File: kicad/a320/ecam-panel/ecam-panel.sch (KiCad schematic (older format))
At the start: 45 parts, among them P1 CONN_02X04, SW1 SW_PUSH_SMALL, SW10 SW_PUSH_SMALL, SW11 SW_PUSH_SMALL, SW12 SW_PUSH_SMALL, SW13 SW_PUSH_SMALL, SW14 SW_PUSH_SMALL, SW15 SW_PUSH_SMALL, SW16 SW_PUSH_SMALL, SW17 SW_PUSH_SMALL_H, SW18 SW_PUSH_SMALL_H, SW2 SW_PUSH_SMALL, SW3 SW_PUSH_SMALL, SW4 SW_PUSH_SMALL, SW5 SW_PUSH_SMALL, SW6 SW_PUSH_SMALL, SW7 SW_PUSH_SMALL, SW8 SW_PUSH_SMALL, SW9 SW_PUSH_SMALL, U1 CD4021, U2 74922, U3 MAX7219

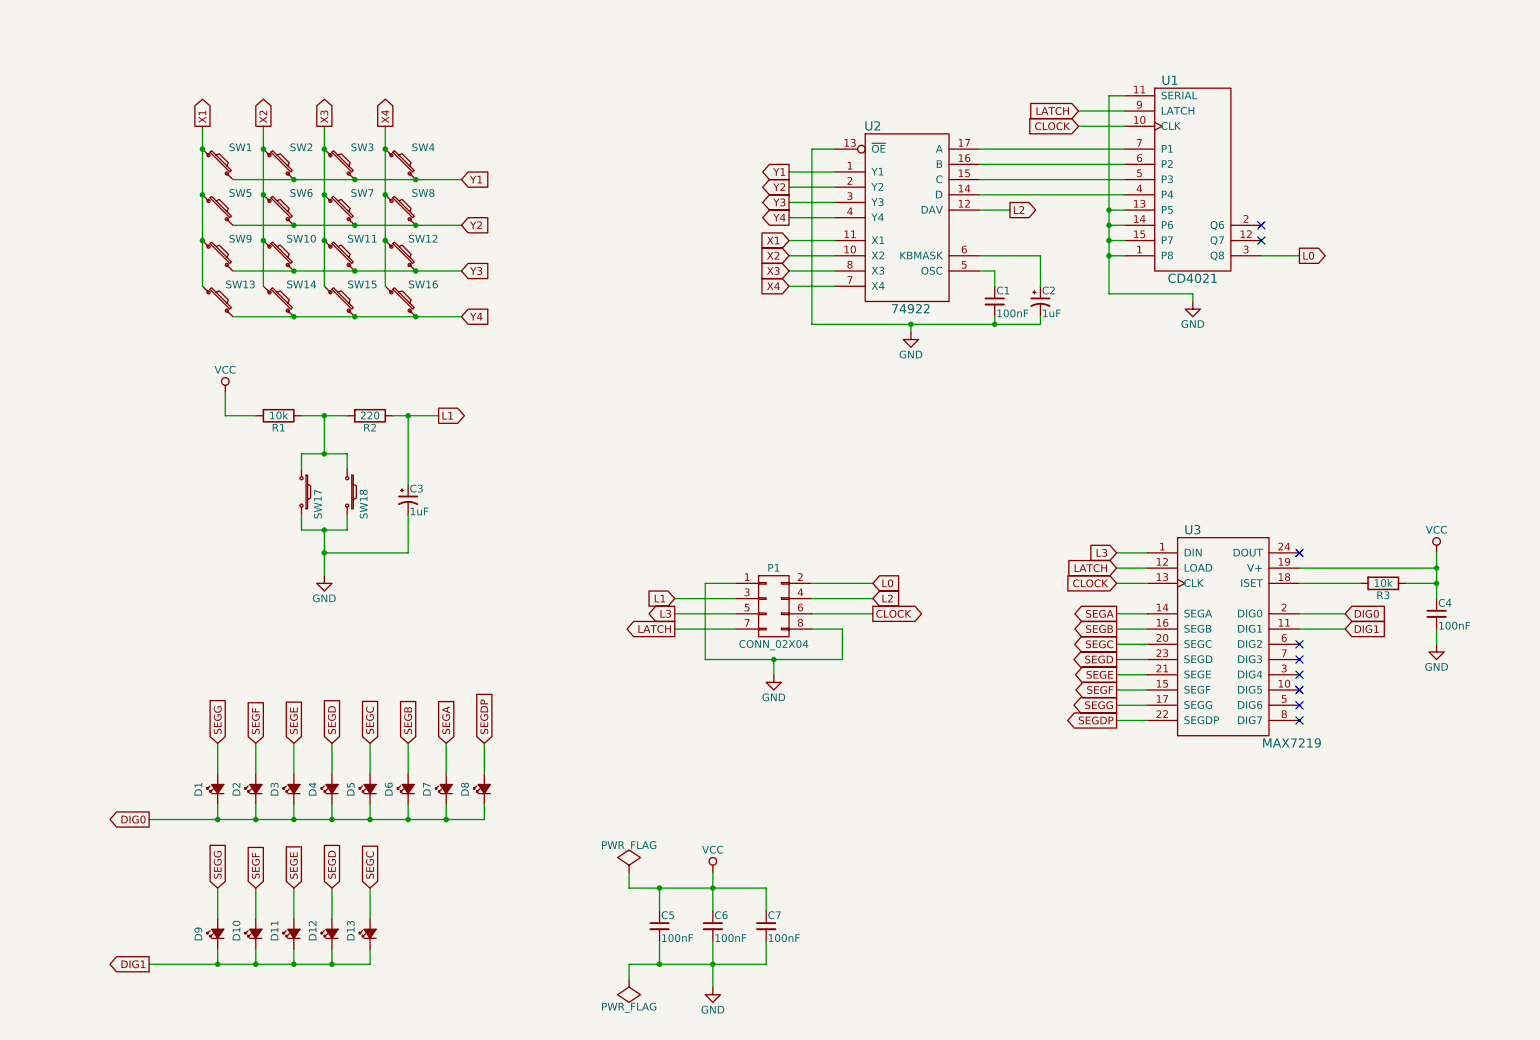
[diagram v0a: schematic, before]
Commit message: Add potentiometers to control ECAM display bright
And also, reorganize the schematic to separate the different subsets of components.
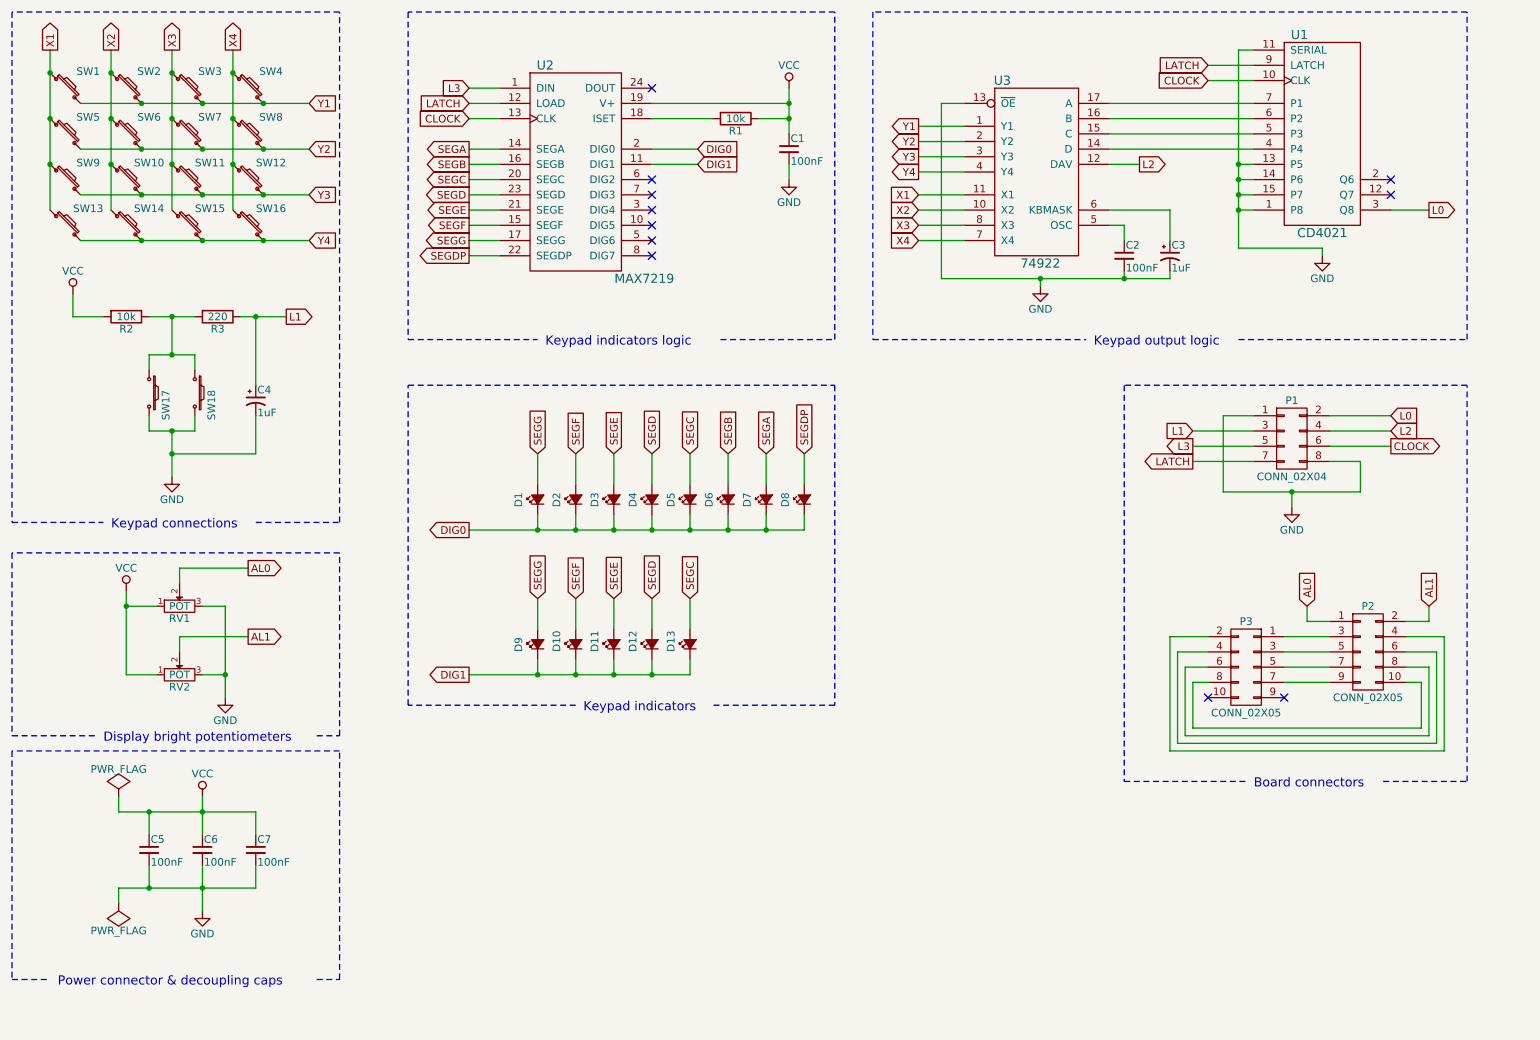
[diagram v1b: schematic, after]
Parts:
- added P2, P3: CONN_02X05, symbol CONN_02X05
- added RV1, RV2: POT, symbol POT
- renumbered C4 to C1, C1 to C2, C2 to C3, C3 to C4, R3 to R1, R1 to R2, R2 to R3, U3 to U2, U2 to U3
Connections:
- net GND: now also RV1.3, RV2.3
- net VCC: now also RV1.1, RV2.1
- new net: P2.10 (P10), P3.8 (P8)
- new net: P2.3 (P3), P3.1 (P1)
- new net: P2.4 (P4), P3.2 (P2)
- new net: P2.5 (P5), P3.3 (P3)
- new net: P2.6 (P6), P3.4 (P4)
- new net: P2.7 (P7), P3.5 (P5)
- new net: P2.8 (P8), P3.6 (P6)
- new net: P2.9 (P9), P3.7 (P7)
- new net AL0: P2.1 (P1), RV1.2
- new net AL1: P2.2 (P2), RV2.2
- no-connect marks 9 -> 11
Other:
- note added: "Board connectors"
- note added: "Display bright potentiometers"
- note added: "Keypad connections"
- note added: "Keypad indicators"
- note added: "Keypad indicators logic"
- note added: "Keypad output logic"
- note added: "Power connector & decoupling caps"
- moved on the sheet: C1, C2, C3, C4, C5, C6, C7, D1, D10, D11, D12, D13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

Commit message: Add backlighting LEDs and power connectors to ECAM panel
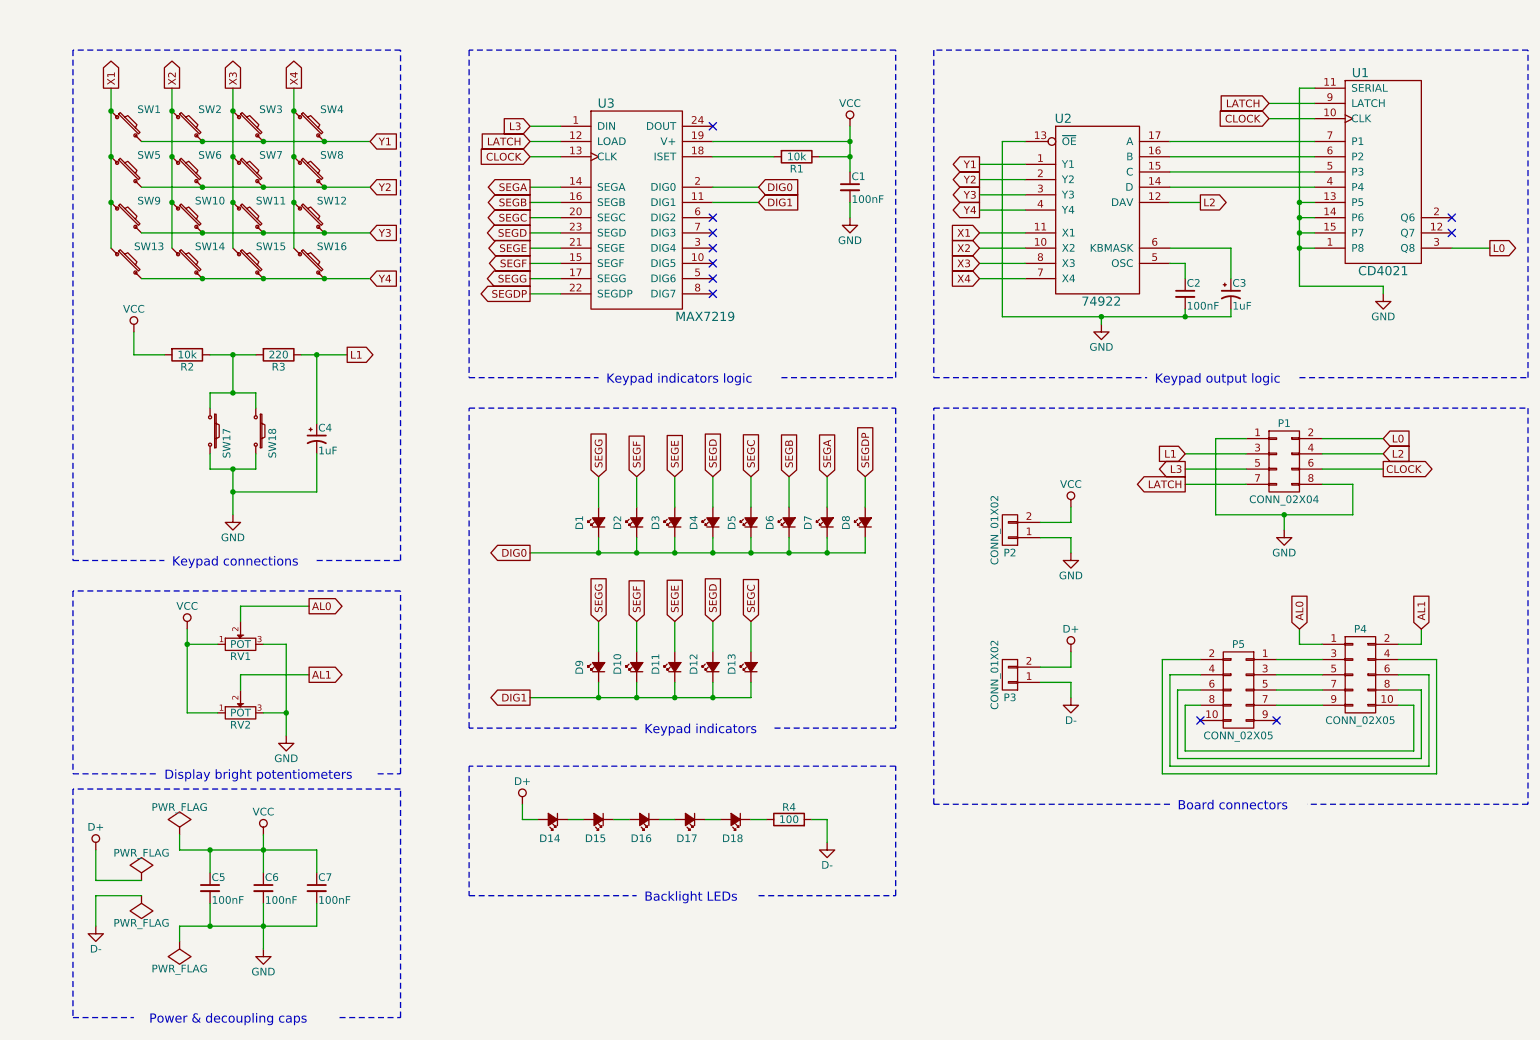
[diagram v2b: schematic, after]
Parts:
- added D14, D15, D16, D17, D18: Led_Small, symbol Led_Small
- added P2, P3: CONN_01X02, symbol CONN_01X02
- added R4: 100, symbol R
- renumbered P2 to P4, P3 to P5, U3 to U2, U2 to U3
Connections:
- net GND: now also P2.1 (P1)
- net VCC: now also P2.2 (P2)
- new net: D14.1 (K), D15.2 (A)
- new net: D15.1 (K), D16.2 (A)
- new net: D16.1 (K), D17.2 (A)
- new net: D18.1 (K), R4.1
- new net: D17.1 (K), D18.2 (A)
- new net D+: D14.2 (A), P3.2 (P2)
- new net D-: P3.1 (P1), R4.2
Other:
- note added: "Backlight LEDs"
- note added: "Power & decoupling caps"
- note removed: "Power connector & decoupling caps"
- moved on the sheet: C1, C2, C3, C4, C5, C6, C7, D1, D10, D11, D12, D13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

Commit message: Add some associations to footprints in A320 ECAM panel
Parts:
- C1, C2, C5, C6, C7: footprint (none) -> avionica:Disc_capacitor
- C3, C4: footprint (none) -> avionica:Radial_capacitor
- D1, D10, D11, D12, D13, D2, D3, D4, D5, D6, D7, D8, D9: footprint (none) -> avionica:Pin_Header_1x02
- D14, D15, D16, D17, D18: footprint (none) -> avionica:LED-1210
- P1: footprint (none) -> avionica:idc-8p
- P4, P5: footprint (none) -> avionica:idc-10p
- R1, R2, R3, R4: footprint (none) -> avionica:Axial_resistor
- RV1, RV2: footprint (none) -> avionica:Pin_Header_1x03
- SW1, SW10, SW11, SW12, SW13, SW14, SW15, SW16, SW17, SW18, SW2, SW3, SW4, SW5, SW6, SW7, SW8, SW9: footprint (none) -> avionica:Omron-B3F-12mm

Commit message: Replace power connectors by 3-line ones
One for anode, two for cathode.
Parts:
- removed P2, P3: CONN_01X02, symbol CONN_01X02
- added P2, P3: CONN_01X03, symbol CONN_01X03
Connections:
- net D+: now also P3.1 (P1)
- net D-: now also P3.2 (P2), P3.3 (P3)
- net GND: now also P2.2 (P2), P2.3 (P3)
- net VCC: now also P2.1 (P1)
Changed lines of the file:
@@
 	3800 6500 4900 6500
-$Comp
-L CONN_01X02 P2
-U 1 1 596968F2
-P 7350 4100
-F 0 "P2" H 7350 4250 50  0000 C CNN
-F 1 "CONN_01X02" V 7450 4100 50  0000 C CNN
-F 2 "" H 7350 4100 50  0001 C CNN
-F 3 "" H 7350 4100 50  0000 C CNN
-	1    7350 4100
-	-1   0    0    1
-$EndComp
-$Comp
-L CONN_01X02 P3
-U 1 1 596969E3
-P 7350 5050
-F 0 "P3" H 7350 5200 50  0000 C CNN
-F 1 "CONN_01X02" V 7450 5050 50  0000 C CNN
-F 2 "" H 7350 5050 50  0001 C CNN
-F 3 "" H 7350 5050 50  0000 C CNN
-	1    7350 5050
-	-1   0    0    1
-$EndComp
 $Comp
 L VCC #PWR020
@@
 L GND #PWR021
 U 1 1 59696FAF
-P 7750 4250
-F 0 "#PWR021" H 7750 4000 50  0001 C CNN
-F 1 "GND" H 7750 4100 50  0000 C CNN
-F 2 "" H 7750 4250 50  0000 C CNN
-F 3 "" H 7750 4250 50  0000 C CNN
-	1    7750 4250
+P 7750 4400
+F 0 "#PWR021" H 7750 4150 50  0001 C CNN
+F 1 "GND" H 7750 4250 50  0000 C CNN
+F 2 "" H 7750 4400 50  0000 C CNN
+F 3 "" H 7750 4400 50  0000 C CNN
+	1    7750 4400
 	1    0    0    -1
 $EndComp
@@
 L D- #PWR023
 U 1 1 5969711B
-P 7750 5200
-F 0 "#PWR023" H 7750 4950 50  0001 C CNN
-F 1 "D-" H 7750 5050 50  0000 C CNN
-F 2 "" H 7750 5200 50  0000 C CNN
-F 3 "" H 7750 5200 50  0000 C CNN
-	1    7750 5200
+P 7750 5350
+F 0 "#PWR023" H 7750 5100 50  0001 C CNN
+F 1 "D-" H 7750 5200 50  0000 C CNN
+F 2 "" H 7750 5350 50  0000 C CNN
+F 3 "" H 7750 5350 50  0000 C CNN
+	1    7750 5350
 	1    0    0    -1
 $EndComp
@@
 	7550 4150 7750 4150
 Wire Wire Line
-	7750 4150 7750 4250
+	7750 4150 7750 4400
 Wire Wire Line
 	7750 3950 7750 4050
@@
 	7550 5100 7750 5100
 Wire Wire Line
-	7750 5100 7750 5200
+	7750 5100 7750 5350
 Wire Notes Line
 	6850 5900 6850 3300
@@
 Wire Notes Line
 	8400 5900 6850 5900
+$Comp
+L CONN_01X03 P2
+U 1 1 5968BBC7
+P 7350 4150
+F 0 "P2" H 7350 4350 50  0000 C CNN
+F 1 "CONN_01X03" V 7450 4150 50  0000 C CNN
+F 2 "" H 7350 4150 50  0000 C CNN
+F 3 "" H 7350 4150 50  0000 C CNN
+	1    7350 4150
+	-1   0    0    -1
+$EndComp
+$Comp
+L CONN_01X03 P3
+U 1 1 5968BDE2
+P 7350 5100
+F 0 "P3" H 7350 5300 50  0000 C CNN
+F 1 "CONN_01X03" V 7450 5100 50  0000 C CNN
+F 2 "" H 7350 5100 50  0000 C CNN
+F 3 "" H 7350 5100 50  0000 C CNN
+	1    7350 5100
+	-1   0    0    -1
+$EndComp
+Wire Wire Line
+	7750 4250 7550 4250
+Connection ~ 7750 4250
+Wire Wire Line
+	7550 5200 7750 5200
+Connection ~ 7750 5200
 $EndSCHEMATC

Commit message: Add the remaining footprint associations in A320 ECAM panel
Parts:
- P2, P3: footprint (none) -> avionica:Jack_55_21
- U1: footprint (none) -> avionica:DIP-16
- U2: footprint (none) -> avionica:DIP-18
- U3: footprint (none) -> avionica:DIP-24
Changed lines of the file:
@@
 F 0 "U3" H 4700 3100 60  0000 C CNN
 F 1 "MAX7219" H 5350 1700 60  0000 C CNN
-F 2 "" H 5050 1400 60  0001 C CNN
+F 2 "avionica:DIP-24" H 5050 1400 60  0001 C CNN
 F 3 "" H 5050 1400 60  0001 C CNN
 	1    4900 2200
@@
 F 0 "U2" H 7700 2800 60  0000 C CNN
 F 1 "74922" H 7950 1600 60  0000 C CNN
-F 2 "" H 7950 2100 60  0001 C CNN
+F 2 "avionica:DIP-18" H 7950 2100 60  0001 C CNN
 F 3 "" H 7950 2100 60  0001 C CNN
 	1    7950 2100
@@
 F 0 "U1" H 9650 2400 60  0000 C CNN
 F 1 "CD4021" H 9800 1100 60  0000 C CNN
-F 2 "" H 9750 1550 60  0001 C CNN
+F 2 "avionica:DIP-16" H 9750 1550 60  0001 C CNN
 F 3 "" H 9750 1550 60  0001 C CNN
 	1    9800 1750
@@
 F 0 "P2" H 7350 4350 50  0000 C CNN
 F 1 "CONN_01X03" V 7450 4150 50  0000 C CNN
-F 2 "" H 7350 4150 50  0000 C CNN
+F 2 "avionica:Jack_55_21" H 7350 4150 50  0001 C CNN
 F 3 "" H 7350 4150 50  0000 C CNN
 	1    7350 4150
@@
 F 0 "P3" H 7350 5300 50  0000 C CNN
 F 1 "CONN_01X03" V 7450 5100 50  0000 C CNN
-F 2 "" H 7350 5100 50  0000 C CNN
+F 2 "avionica:Jack_55_21" H 7350 5100 50  0001 C CNN
 F 3 "" H 7350 5100 50  0000 C CNN
 	1    7350 5100

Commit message: Make the VCC pin non-visible in MAX7219
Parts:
- removed C1: 100nF, avionica:Disc_capacitor, symbol C_Small
- renumbered C2 to C1, C3 to C2, C4 to C3, C5 to C4, C6 to C5, C7 to C6
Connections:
- net VCC: no longer U3.19 (V+)
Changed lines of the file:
@@
 Y4
 $Comp
-L C_Small C2
+L C_Small C1
 U 1 1 5951E730
 P 8500 2550
-F 0 "C2" H 8510 2620 50  0000 L CNN
+F 0 "C1" H 8510 2620 50  0000 L CNN
 F 1 "100nF" H 8510 2470 50  0000 L CNN
 F 2 "avionica:Disc_capacitor" H 8500 2550 50  0001 C CNN
@@
 	0    1    1    0
 $EndComp
-$Comp
-L C_Small C1
-U 1 1 5952D81F
-P 6300 1850
-F 0 "C1" H 6310 1920 50  0000 L CNN
-F 1 "100nF" H 6310 1770 50  0000 L CNN
-F 2 "avionica:Disc_capacitor" H 6300 1850 50  0001 C CNN
-F 3 "" H 6300 1850 50  0000 C CNN
-	1    6300 1850
-	1    0    0    -1
-$EndComp
-Wire Wire Line
-	6300 2050 6300 1950
-Wire Wire Line
-	6300 1450 6300 1750
 Wire Wire Line
 	6300 1650 6100 1650
 Wire Wire Line
 	5800 1650 5400 1650
-Wire Wire Line
-	5400 1550 6300 1550
-Connection ~ 6300 1650
-Connection ~ 6300 1550
 $Comp
 L SW_PUSH_SMALL_H SW18
@@
 Connection ~ 9250 1950
 $Comp
-L C_Small C6
+L C_Small C5
 U 1 1 5953F9B6
 P 2450 6450
-F 0 "C6" H 2460 6520 50  0000 L CNN
+F 0 "C5" H 2460 6520 50  0000 L CNN
 F 1 "100nF" H 2460 6370 50  0000 L CNN
 F 2 "avionica:Disc_capacitor" H 2450 6450 50  0001 C CNN
@@
 $EndComp
 $Comp
-L C_Small C5
+L C_Small C4
 U 1 1 5953FC97
 P 2100 6450
-F 0 "C5" H 2110 6520 50  0000 L CNN
+F 0 "C4" H 2110 6520 50  0000 L CNN
 F 1 "100nF" H 2110 6370 50  0000 L CNN
 F 2 "avionica:Disc_capacitor" H 2100 6450 50  0001 C CNN
@@
 $EndComp
 $Comp
-L C_Small C7
+L C_Small C6
 U 1 1 5953FD35
 P 2800 6450
-F 0 "C7" H 2810 6520 50  0000 L CNN
+F 0 "C6" H 2810 6520 50  0000 L CNN
 F 1 "100nF" H 2810 6370 50  0000 L CNN
 F 2 "avionica:Disc_capacitor" H 2800 6450 50  0001 C CNN
@@
 $EndComp
 $Comp
-L GND #PWR010
-U 1 1 59543FF4
-P 6300 2050
-F 0 "#PWR010" H 6300 1800 50  0001 C CNN
-F 1 "GND" H 6300 1900 50  0000 C CNN
-F 2 "" H 6300 2050 50  0000 C CNN
-F 3 "" H 6300 2050 50  0000 C CNN
-	1    6300 2050
-	1    0    0    -1
-$EndComp
-$Comp
 L VCC #PWR011
 U 1 1 595440B4
@@
 $EndComp
 $Comp
-L CP1_Small C4
+L CP1_Small C3
 U 1 1 595770B6
 P 2800 3500
-F 0 "C4" H 2810 3570 50  0000 L CNN
+F 0 "C3" H 2810 3570 50  0000 L CNN
 F 1 "1uF" H 2810 3420 50  0000 L CNN
 F 2 "avionica:Radial_capacitor" H 2800 3500 50  0001 C CNN
@@
 $EndComp
 $Comp
-L CP1_Small C3
+L CP1_Small C2
 U 1 1 5958C1F6
 P 8800 2550
-F 0 "C3" H 8810 2620 50  0000 L CNN
+F 0 "C2" H 8810 2620 50  0000 L CNN
 F 1 "1uF" H 8810 2470 50  0000 L CNN
 F 2 "avionica:Radial_capacitor" H 8800 2550 50  0001 C CNN
@@
 	1    0    0    -1
 $EndComp
+Wire Wire Line
+	6300 1650 6300 1450
 $EndSCHEMATC

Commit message: Adjust footprints layout in A320 ECAM panel
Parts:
- added D14: Led_Small, avionica:Pin_Header_1x02, symbol Led_Small
- renumbered D14 to D15, D15 to D16, D16 to D17, D17 to D18, D18 to D19
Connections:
- net DIG1: now also D14.1 (K)
- net SEGB: now also D14.2 (A)
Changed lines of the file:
@@
 LIBS:contrib
 LIBS:valves
-LIBS:ecam-panel-cache
 EELAYER 25 0
 EELAYER END
@@
 	5650 5200 5650 5100
 Wire Wire Line
-	4200 5200 5650 5200
+	4200 5200 5900 5200
 Wire Wire Line
 	5400 5100 5400 5200
@@
 	9250 3100 10750 3100
 $Comp
-L Led_Small D14
+L Led_Small D15
 U 1 1 59682439
 P 4350 6000
-F 0 "D14" H 4300 6125 50  0000 L CNN
+F 0 "D15" H 4300 6125 50  0000 L CNN
 F 1 "Led_Small" H 4175 5900 50  0001 L CNN
 F 2 "avionica:LED-1210" V 4350 6000 50  0001 C CNN
@@
 $EndComp
 $Comp
-L Led_Small D15
+L Led_Small D16
 U 1 1 59687653
 P 4650 6000
-F 0 "D15" H 4600 6125 50  0000 L CNN
+F 0 "D16" H 4600 6125 50  0000 L CNN
 F 1 "Led_Small" H 4475 5900 50  0001 L CNN
 F 2 "avionica:LED-1210" V 4650 6000 50  0001 C CNN
@@
 $EndComp
 $Comp
-L Led_Small D16
+L Led_Small D17
 U 1 1 5968770B
 P 4950 6000
-F 0 "D16" H 4900 6125 50  0000 L CNN
+F 0 "D17" H 4900 6125 50  0000 L CNN
 F 1 "Led_Small" H 4775 5900 50  0001 L CNN
 F 2 "avionica:LED-1210" V 4950 6000 50  0001 C CNN
@@
 	6150 6000 6050 6000
 $Comp
-L Led_Small D17
+L Led_Small D18
 U 1 1 59689C60
 P 5250 6000
-F 0 "D17" H 5200 6125 50  0000 L CNN
+F 0 "D18" H 5200 6125 50  0000 L CNN
 F 1 "Led_Small" H 5075 5900 50  0001 L CNN
 F 2 "avionica:LED-1210" V 5250 6000 50  0001 C CNN
@@
 $EndComp
 $Comp
-L Led_Small D18
+L Led_Small D19
 U 1 1 59689D1E
 P 5550 6000
-F 0 "D18" H 5500 6125 50  0000 L CNN
+F 0 "D19" H 5500 6125 50  0000 L CNN
 F 1 "Led_Small" H 5375 5900 50  0001 L CNN
 F 2 "avionica:LED-1210" V 5550 6000 50  0001 C CNN
@@
 Wire Wire Line
 	6300 1650 6300 1450
+Text GLabel 5900 4700 1    50   Input ~ 0
+SEGB
+$Comp
+L Led_Small D14
+U 1 1 597B8575
+P 5900 5000
+F 0 "D14" H 5850 5125 50  0000 L CNN
+F 1 "Led_Small" H 5725 4900 50  0001 L CNN
+F 2 "avionica:Pin_Header_1x02" V 5900 5000 50  0001 C CNN
+F 3 "" V 5900 5000 50  0000 C CNN
+	1    5900 5000
+	0    -1   -1   0
+$EndComp
+Wire Wire Line
+	5900 4700 5900 4900
+Wire Wire Line
+	5900 5200 5900 5100
+Connection ~ 5650 5200
 $EndSCHEMATC
